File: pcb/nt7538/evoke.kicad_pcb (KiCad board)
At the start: 2 copper layers, 60 x 45 mm, 19 parts, among them U1 STM32F103C8Tx

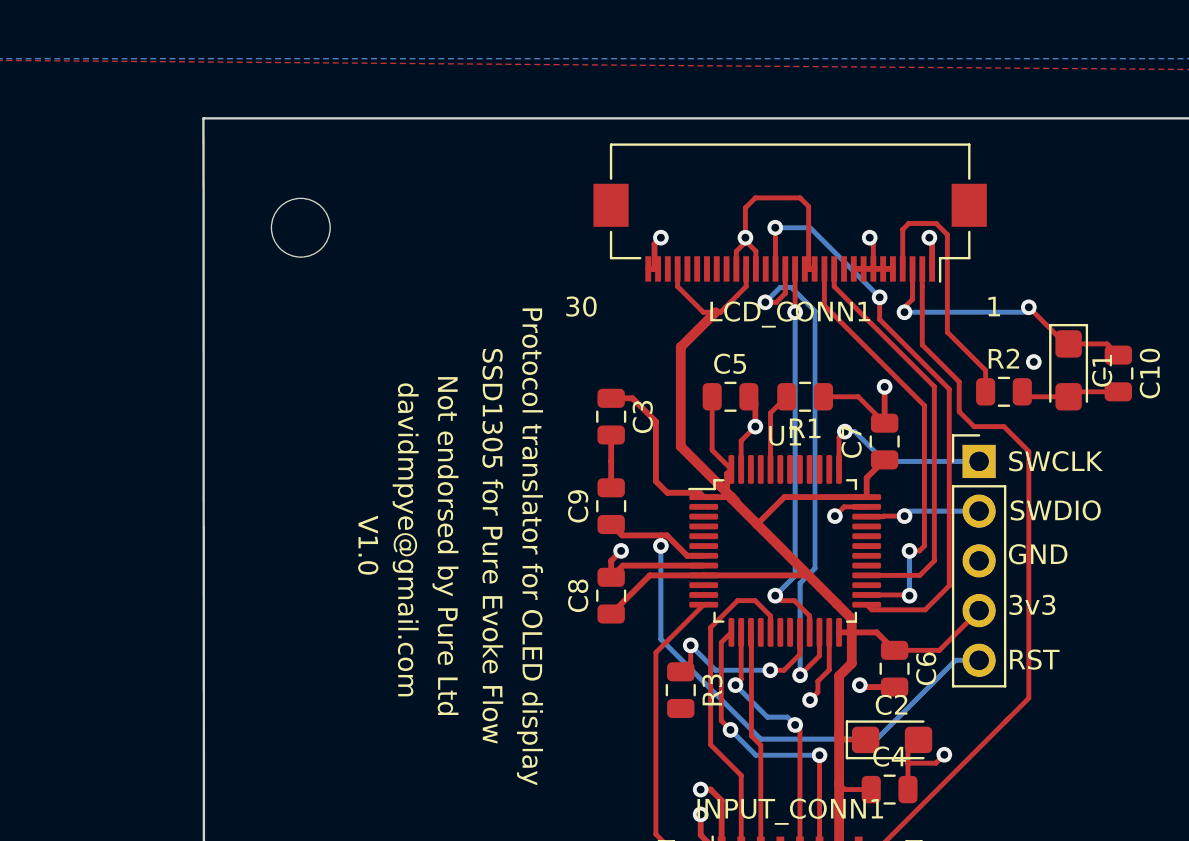
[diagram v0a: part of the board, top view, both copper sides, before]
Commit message: Initial changes for LCD support
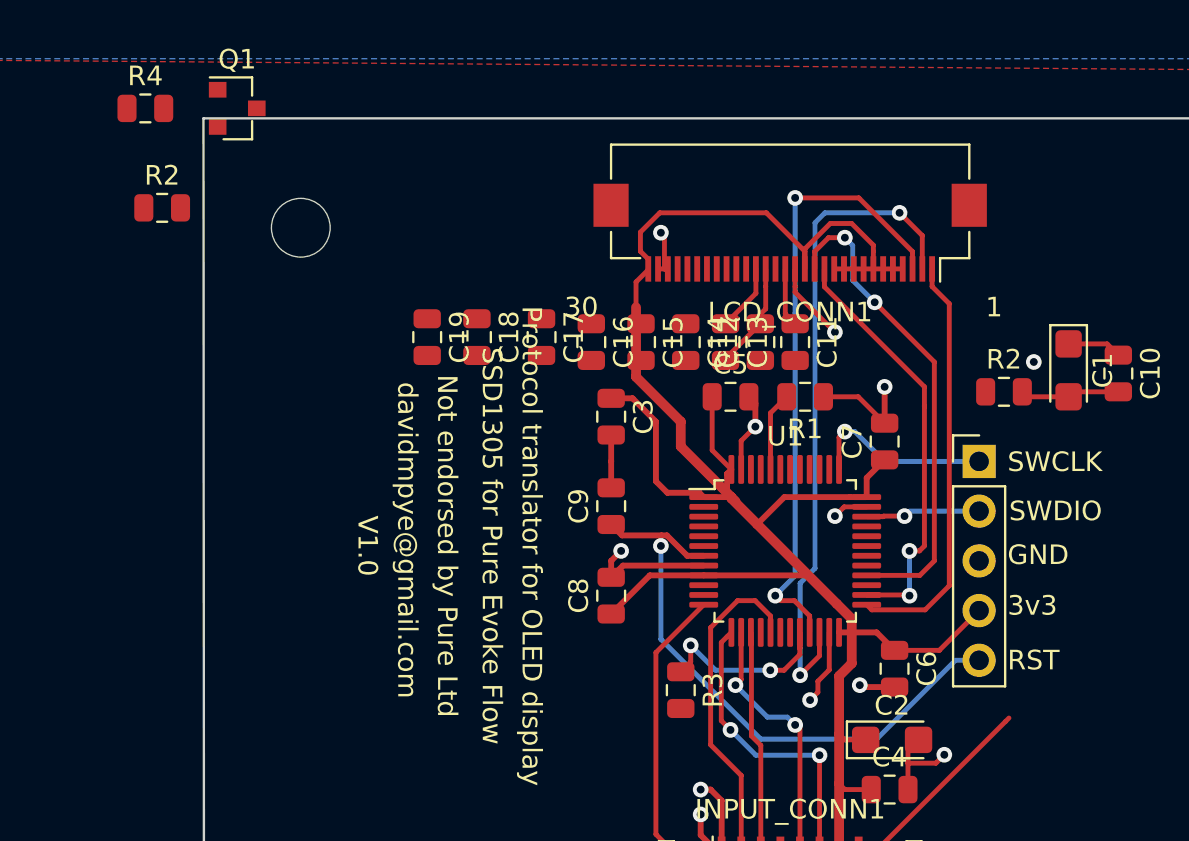
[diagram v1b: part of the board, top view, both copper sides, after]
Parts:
- added C11: 1uF, Capacitor_SMD:C_0805_2012Metric, F.Cu at (105.2, 42.9)
- added C12: 1uF, Capacitor_SMD:C_0805_2012Metric, F.Cu at (103.4, 42.9)
- added C13: 1uF, Capacitor_SMD:C_0805_2012Metric, F.Cu at (101.6, 42.9)
- added C14: 1uF, Capacitor_SMD:C_0805_2012Metric, F.Cu at (99.6, 42.9)
- added C15: 1uF, Capacitor_SMD:C_0805_2012Metric, F.Cu at (97.3, 42.9)
- added C16: 1uF, Capacitor_SMD:C_0805_2012Metric, F.Cu at (94.7, 42.9)
- added C17: 1uF, Capacitor_SMD:C_0805_2012Metric, F.Cu at (92.2, 42.7)
- added C18: 1uF, Capacitor_SMD:C_0805_2012Metric, F.Cu at (88.9, 42.7)
- added C19: 1uF, Capacitor_SMD:C_0805_2012Metric, F.Cu at (86.4, 42.7)
- added Q1: AO3400A, Package_TO_SOT_SMD:SOT-23, F.Cu at (76.7, 31.0)
- added R2: 500R, Resistor_SMD:R_0805_2012Metric, F.Cu at (72.8, 36.1)
- added R4: 200K, Resistor_SMD:R_0805_2012Metric, F.Cu at (72.0, 31.0)
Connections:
- C1 pad 1: Net-(C1-Pad1) -> +3V3
- C10 pad 1: Net-(C1-Pad1) -> +3V3
- LCD_CONN1 pad 1: GND -> LCD_CS
- LCD_CONN1 pad 10: Net-(LCD_CONN1-Pad10) -> +3V3
- LCD_CONN1 pad 11: LCD_DATA -> +3V3
- LCD_CONN1 pad 13: GND -> LCD_DATA
- LCD_CONN1 pad 14: GND -> +3V3
- LCD_CONN1 pad 15: LCD_D_C -> GND
- LCD_CONN1 pad 16: LCD_RST -> Net-(C11-Pad1)
- LCD_CONN1 pad 17: LCD_CS -> Net-(C12-Pad1)
- LCD_CONN1 pad 19: GND -> Net-(C13-Pad1)
- LCD_CONN1 pad 2: VCC -> LCD_RST
- LCD_CONN1 pad 20: +3V3 -> Net-(C14-Pad2)
- LCD_CONN1 pad 21: GND -> Net-(C14-Pad1)
- LCD_CONN1 pad 27: +3V3 -> Net-(LCD_CONN1-Pad27)
- LCD_CONN1 pad 28: Net-(LCD_CONN1-Pad28) -> GND
- LCD_CONN1 pad 3: Net-(C1-Pad1) -> LCD_D_C
- LCD_CONN1 pad 30: GND -> +3V3
- LCD_CONN1 pad 4: Net-(LCD_CONN1-Pad4) -> +3V3
- LCD_CONN1 pad 5: GND -> +3V3
- LCD_CONN1 pad 6: GND -> +3V3
- LCD_CONN1 pad 7: GND -> +3V3
- LCD_CONN1 pad 8: GND -> +3V3
- LCD_CONN1 pad 9: GND -> +3V3
- U1 pad 10: Net-(U1-Pad10) -> LCD_BACKLIGHT_PWM
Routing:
- net VCC: track 37.4 -> 10.4 mm
- net +3V3: track 88.8 -> 110.4 mm
- net Net-(C1-Pad1): track 14.6 -> 0.00 mm, vias 2 -> 0
- net Net-(LCD_CONN1-Pad4): track 13.5 -> 0.00 mm
- net GND: track 62.0 -> 48.7 mm, vias 14 -> 12
- net LCD_D_C: track 20.1 -> 32.0 mm
- net LCD_CS: track 30.0 -> 21.4 mm, vias 2 -> 0
- net LCD_RST: track 27.3 -> 33.9 mm
- net Net-(C12-Pad2): track 0.00 -> 5.53 mm
- net LCD_DATA: track 20.8 -> 24.9 mm, vias 0 -> 2
- net Net-(C13-Pad1): track 0.00 -> 3.44 mm
- net Net-(C11-Pad1): track 0.00 -> 3.01 mm

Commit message: Further evolution of NT schmatic
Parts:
- moved R4 37.1 mm to (91.2, 62.7), turned to 90 degrees
- moved Q1 36.5 mm to (94.7, 62.7)
- moved R2 32.0 mm to (95.0, 59.2)
- moved C19 5.93 mm to (92.2, 43.7)
- moved C18 5.68 mm to (94.5, 43.7)
- moved C17 4.68 mm to (96.8, 43.7)
- moved C11 4.64 mm to (109.7, 43.7)
- moved C12 4.38 mm to (107.7, 43.7), turned to 270 degrees
- moved C16 4.13 mm to (98.8, 43.7)
- moved C13 3.89 mm to (105.4, 43.7), turned to 90 degrees
- moved C14 3.65 mm to (103.1, 43.8), turned to 90 degrees
- moved C15 3.64 mm to (100.8, 43.7)
- moved C5 1.02 mm to (101.9, 46.7)
- moved R1 1.02 mm to (105.7, 46.7)
- moved C3 0.84 mm to (95.8, 47.6)
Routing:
- net +3V3: track 110.4 -> 139.0 mm
- net GND: track 48.7 -> 68.5 mm, vias 12 -> 11
- net VCC: track 10.4 -> 0.00 mm
- net Net-(C19-Pad1): track 0.00 -> 9.47 mm
- net Net-(C18-Pad1): track 0.00 -> 8.24 mm
- net Net-(C14-Pad1): track 0.00 -> 6.86 mm
- net Net-(C17-Pad1): track 0.00 -> 6.65 mm
- net LCD_BACKLIGHT_PWM: track 0.00 -> 6.55 mm
- net Net-(C12-Pad1): track 0.00 -> 5.80 mm
- net Net-(C14-Pad2): track 0.00 -> 5.62 mm
- net Net-(Q1-Pad1): track 0.00 -> 5.30 mm
- net Net-(C11-Pad1): track 3.01 -> 8.15 mm
- net Net-(C16-Pad1): track 0.00 -> 4.59 mm
- net Net-(C15-Pad1): track 0.00 -> 3.90 mm
- net Net-(C13-Pad1): track 3.44 -> 6.78 mm
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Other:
- board text added: "Protocol translator for LCD display"
- board text added: "for Pure Evoke Flow"
- board text removed: "Protocol translator for OLED display"
- board text removed: "SSD1305 for Pure Evoke Flow"

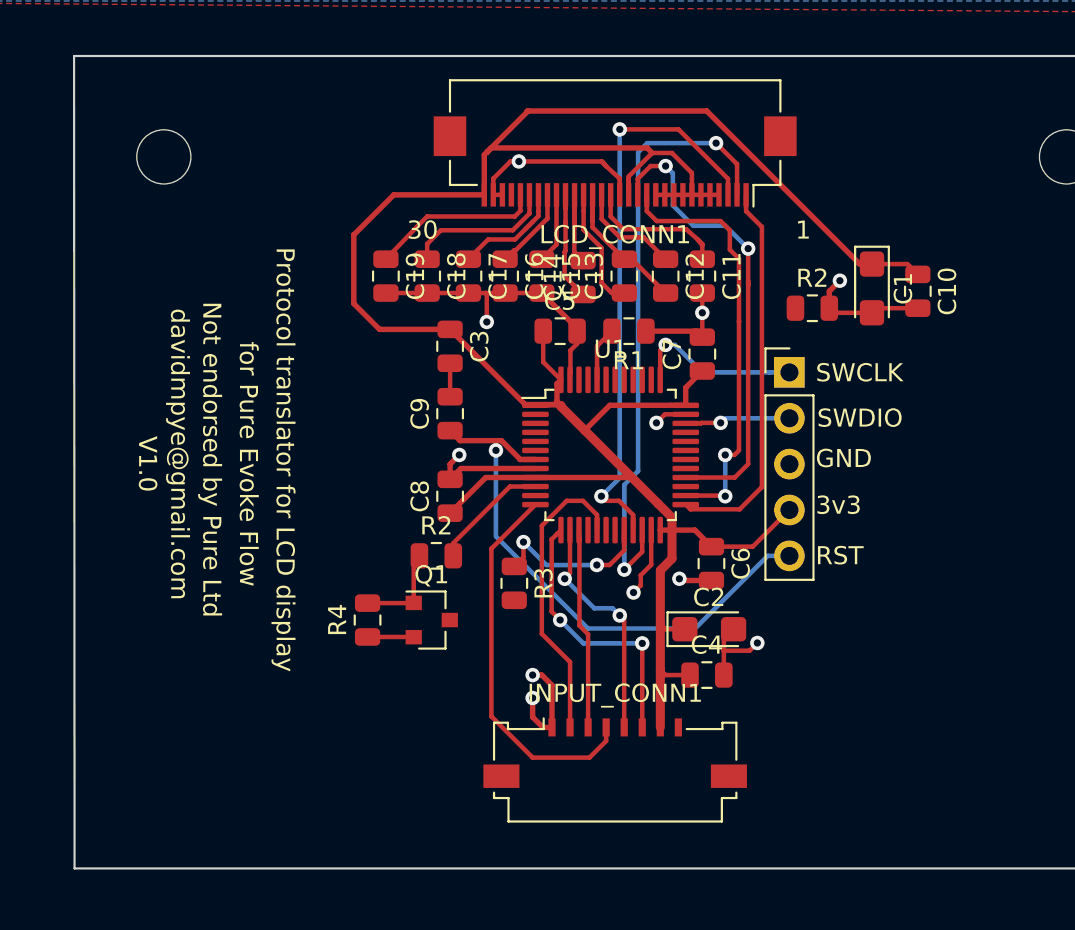
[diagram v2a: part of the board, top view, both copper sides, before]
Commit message: Put next revision into manufacture - hopefully ready to go, now with test points!
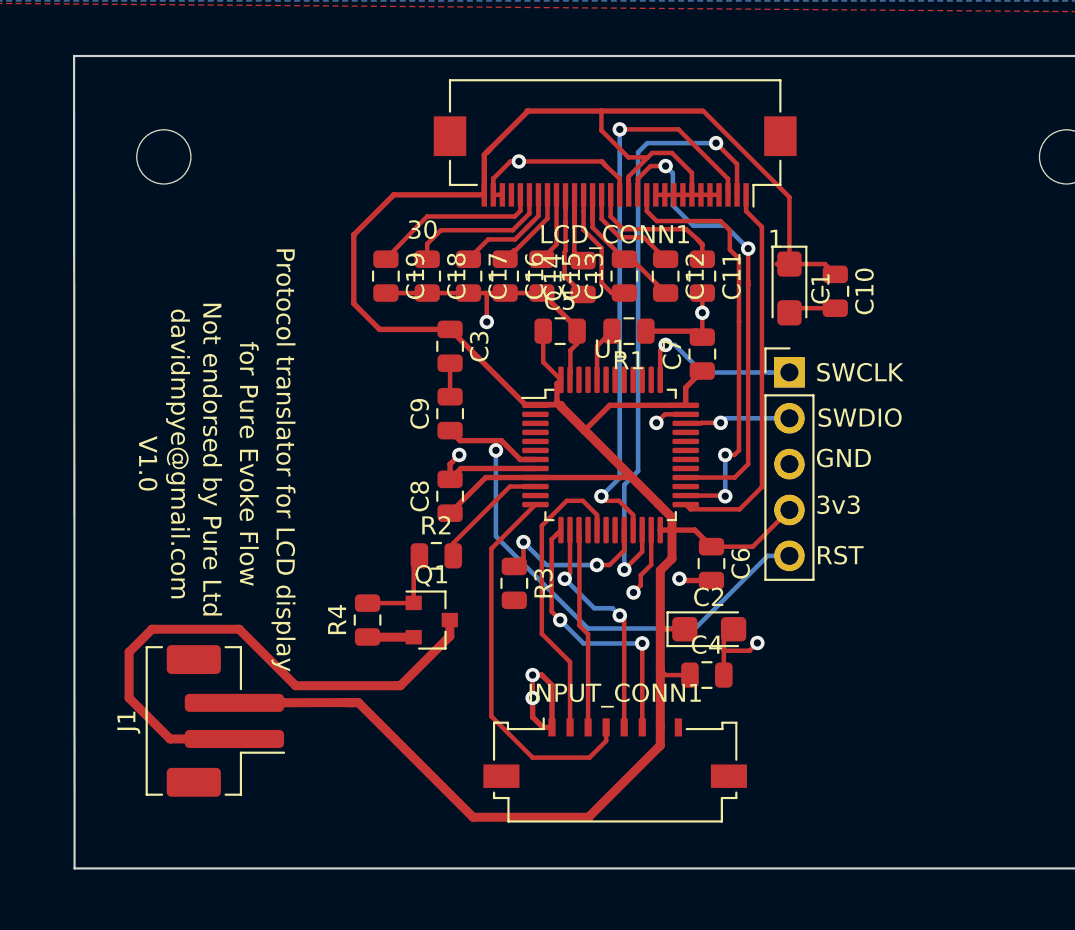
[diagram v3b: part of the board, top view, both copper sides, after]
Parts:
- removed the R2 at (115.8, 45.5)
- added J1: Conn_01x02_Male, Connector_JST:JST_PH_B2B-PH-SM4-TB_1x02-1MP_P2.00mm_Vertical, F.Cu at (83.3, 68.3)
- moved C1 4.57 mm to (114.6, 44.4)
- moved C10 4.57 mm to (117.1, 44.5)
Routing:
- net Net-(J1-Pad1): track 0.00 -> 30.9 mm
- net +3V3: track 139.0 -> 164.7 mm
- net GND: track 68.5 -> 65.5 mm, vias 11 -> 10

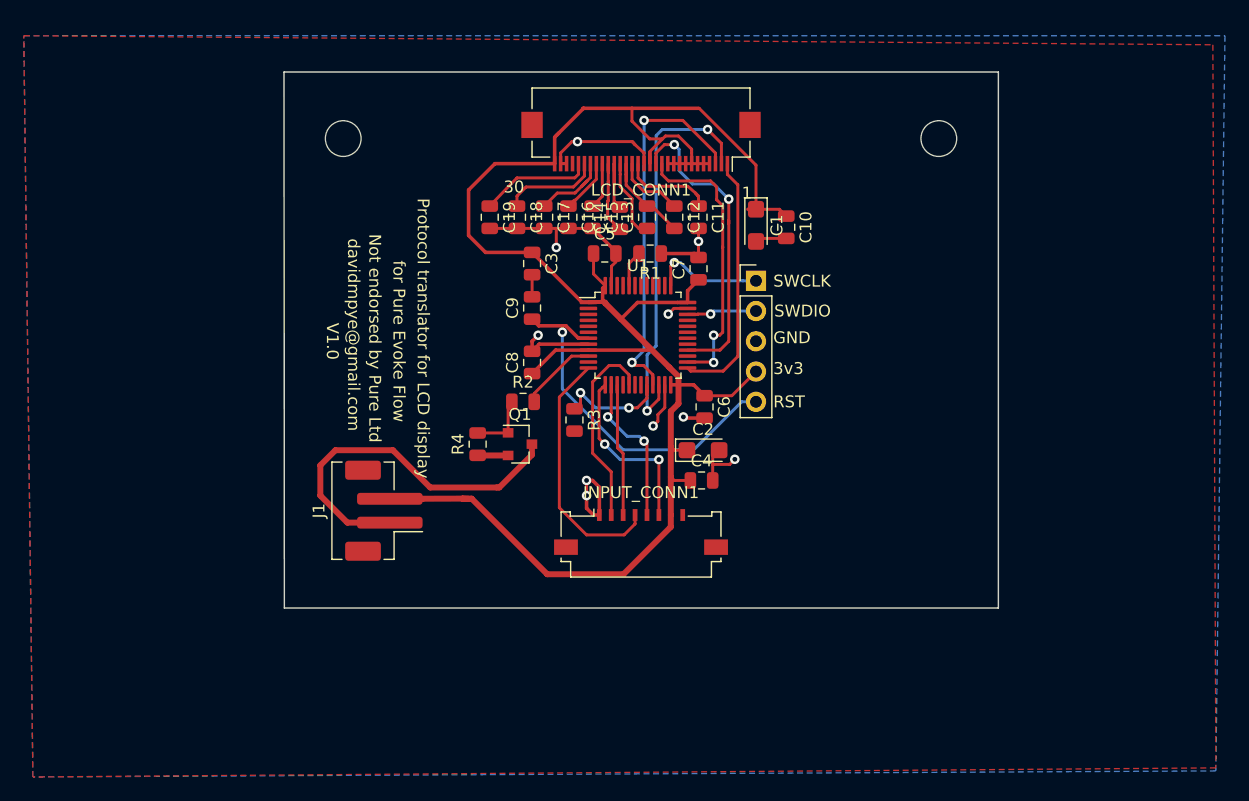
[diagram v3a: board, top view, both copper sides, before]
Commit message: Commit of NT version including trimpot
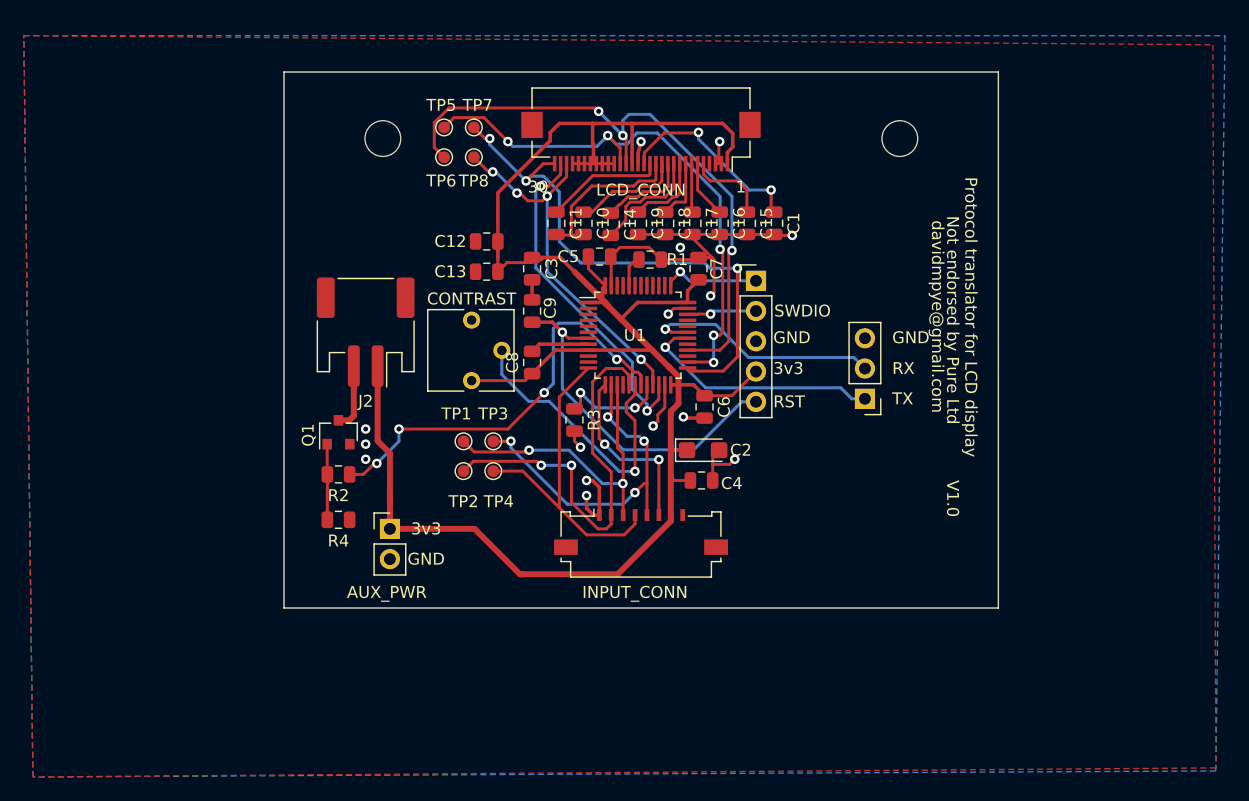
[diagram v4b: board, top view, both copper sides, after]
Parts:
- added AUX_PWR: SUPP_PWR, Connector_PinHeader_2.54mm:PinHeader_1x02_P2.54mm_Vertical, F.Cu at (83.8, 69.8)
- added CONTRAST: 100K, Potentiometer_THT:Potentiometer_Vishay_T73YP_Vertical, F.Cu at (90.7, 57.4)
- added J2: BACKLIGHT_CONN, Connector_JST:JST_PH_S2B-PH-SM4-TB_1x02-1MP_P2.00mm_Horizontal, F.Cu at (81.8, 53.3)
- added TP1: TestPoint, TestPoint:TestPoint_Pad_D1.0mm, F.Cu at (90.0, 62.5)
- added TP2: TestPoint, TestPoint:TestPoint_Pad_D1.0mm, F.Cu at (90.0, 65.0)
- added TP3: TestPoint, TestPoint:TestPoint_Pad_D1.0mm, F.Cu at (92.5, 62.5)
- added TP4: TestPoint, TestPoint:TestPoint_Pad_D1.0mm, F.Cu at (92.5, 65.0)
- added TP5: TestPoint, TestPoint:TestPoint_Pad_D1.0mm, F.Cu at (88.4, 36.1)
- added TP6: TestPoint, TestPoint:TestPoint_Pad_D1.0mm, F.Cu at (88.4, 38.6)
- added TP7: TestPoint, TestPoint:TestPoint_Pad_D1.0mm, F.Cu at (90.9, 36.1)
- added TP8: TestPoint, TestPoint:TestPoint_Pad_D1.0mm, F.Cu at (90.9, 38.6)
- C1: value 10uF -> 1uF; footprint Capacitor_Tantalum_SMD:CP_EIA-3216-18_Kemet-A -> Capacitor_SMD:C_0805_2012Metric
- C10: value 100nF -> 1uF
- C12: value 1uF -> 100nF
- C13: value 1uF -> 4.7uF
- J1: value Conn_01x02_Male -> Conn_01x03_Male; footprint Connector_JST:JST_PH_B2B-PH-SM4-TB_1x02-1MP_P2.00mm_Vertical -> Connector_PinHeader_2.54mm:PinHeader_1x03_P2.54mm_Vertical
- Q1: value AO3400A -> Q_NMOS_GSD
- moved J1 41.5 mm to (123.7, 58.9), turned to 180 degrees
- moved C10 17.0 mm to (100.1, 44.2)
- moved R2 16.7 mm to (79.5, 65.3)
- moved C12 15.9 mm to (91.9, 45.7), turned to 180 degrees
- moved Q1 15.3 mm to (79.5, 61.7), turned to 90 degrees
- moved C13 14.2 mm to (91.9, 48.3), turned to 180 degrees
- moved R4 13.3 mm to (79.5, 69.1), turned to 0 degrees
- moved C15 13.0 mm to (113.8, 44.2)
- moved C16 12.7 mm to (111.5, 44.2)
- moved C17 12.5 mm to (109.2, 44.2)
- moved C18 12.5 mm to (106.9, 44.2)
- moved C19 12.5 mm to (104.6, 44.2)
- moved C11 11.9 mm to (97.8, 44.2)
- moved REF** 3.33 mm to (83.2, 37.1)
- moved REF** 3.27 mm to (126.6, 37.1)
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- renumbered INPUT_CONN1 to INPUT_CONN, LCD_CONN1 to LCD_CONN
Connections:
- C1 pad 1: +3V3 -> Net-(C1-Pad1)
- C10 pad 1: +3V3 -> Net-(C10-Pad1)
- C10 pad 2: GND -> Net-(C10-Pad2)
- C11 pad 2: GND -> Net-(C10-Pad2)
- C12 pad 1: Net-(C12-Pad1) -> +3V3
- C12 pad 2: Net-(C12-Pad2) -> GND
- C13 pad 1: Net-(C13-Pad1) -> +3V3
- C13 pad 2: Net-(C12-Pad2) -> GND
- J1 pad 1: Net-(J1-Pad1) -> USART1_TX
- J1 pad 2: +3V3 -> USART1_RX
- LCD_CONN pad 1: LCD_CS -> +3V3
- LCD_CONN pad 10: +3V3 -> Net-(C14-Pad2)
- LCD_CONN pad 11: +3V3 -> Net-(C14-Pad1)
- LCD_CONN pad 12: LCD_SCK -> Net-(C10-Pad1)
- LCD_CONN pad 13: LCD_DATA -> Net-(C10-Pad2)
- LCD_CONN pad 14: +3V3 -> Net-(C11-Pad1)
- LCD_CONN pad 15: GND -> Net-(C1-Pad1)
- LCD_CONN pad 16: Net-(C11-Pad1) -> GND
- LCD_CONN pad 17: Net-(C12-Pad1) -> +3V3
- LCD_CONN pad 18: Net-(C12-Pad2) -> LCD_DATA
- LCD_CONN pad 19: Net-(C13-Pad1) -> LCD_SCK
- LCD_CONN pad 2: LCD_RST -> GND
- LCD_CONN pad 20: Net-(C14-Pad2) -> +3V3
- LCD_CONN pad 21: Net-(C14-Pad1) -> +3V3
- LCD_CONN pad 22: Net-(C15-Pad1) -> +3V3
- LCD_CONN pad 23: Net-(C16-Pad1) -> +3V3
- LCD_CONN pad 24: Net-(C17-Pad1) -> +3V3
- LCD_CONN pad 25: Net-(C18-Pad1) -> +3V3
- LCD_CONN pad 26: Net-(C19-Pad1) -> +3V3
- LCD_CONN pad 27: Net-(LCD_CONN1-Pad27) -> +3V3
- LCD_CONN pad 28: GND -> LCD_D_C
- LCD_CONN pad 29: GND -> LCD_RST
- LCD_CONN pad 3: LCD_D_C -> GND
- LCD_CONN pad 30: +3V3 -> LCD_CS
- LCD_CONN pad 4: +3V3 -> Net-(LCD_CONN1-Pad4)
- LCD_CONN pad 5: +3V3 -> Net-(C15-Pad1)
- LCD_CONN pad 6: +3V3 -> Net-(C16-Pad1)
- LCD_CONN pad 7: +3V3 -> Net-(C17-Pad1)
- LCD_CONN pad 8: +3V3 -> Net-(C18-Pad1)
- LCD_CONN pad 9: +3V3 -> Net-(C19-Pad1)
- Q1 pad 3: Net-(J1-Pad1) -> Net-(J2-Pad2)
- R4 pad 1: GND -> Net-(Q1-Pad1)
- R4 pad 2: Net-(Q1-Pad1) -> GND
- U1 pad 10: LCD_BACKLIGHT_PWM -> Net-(U1-Pad10)
- U1 pad 19: Net-(U1-Pad19) -> LCD_BACKLIGHT_PWM
- U1 pad 30: Net-(U1-Pad30) -> USART1_TX
- U1 pad 31: Net-(U1-Pad31) -> USART1_RX
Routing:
- net Net-(J1-Pad1): track 30.9 -> 0.00 mm
- net LCD_BACKLIGHT_PWM: track 6.55 -> 35.7 mm, vias 0 -> 4
- net LCD_DATA: track 26.2 -> 53.2 mm, vias 2 -> 3
- net Net-(U1-Pad18): track 0.00 -> 24.5 mm, vias 0 -> 1
- net LCD_CS: track 21.4 -> 45.3 mm, vias 0 -> 3
- net LCD_SCK: track 23.8 -> 47.6 mm, vias 2 -> 5
- net USART1_TX: track 0.00 -> 20.7 mm, vias 0 -> 1
- net USART1_RX: track 0.00 -> 20.4 mm, vias 0 -> 1
- net SDIN_IN: track 16.6 -> 35.1 mm, vias 0 -> 2
- net Net-(C1-Pad1): track 0.00 -> 16.6 mm, vias 0 -> 2
- net CS_IN: track 13.1 -> 29.3 mm, vias 2 -> 4
- net SCK_IN: track 11.1 -> 25.8 mm, vias 0 -> 2
- net Net-(C10-Pad2): track 0.00 -> 14.1 mm
- net Net-(C10-Pad1): track 0.00 -> 9.21 mm
- net Net-(C12-Pad2): track 8.83 -> 0.00 mm
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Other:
- board text added: "RX"
- board text added: "TX"
- board text removed: "SWCLK"
- board text removed: "for Pure Evoke Flow"
